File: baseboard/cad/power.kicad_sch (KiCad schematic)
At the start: 37 parts, among them J6 2P_HEADER, J7 2P_HEADER, U7 TLV767, U8 LT3463, U9 LT3032

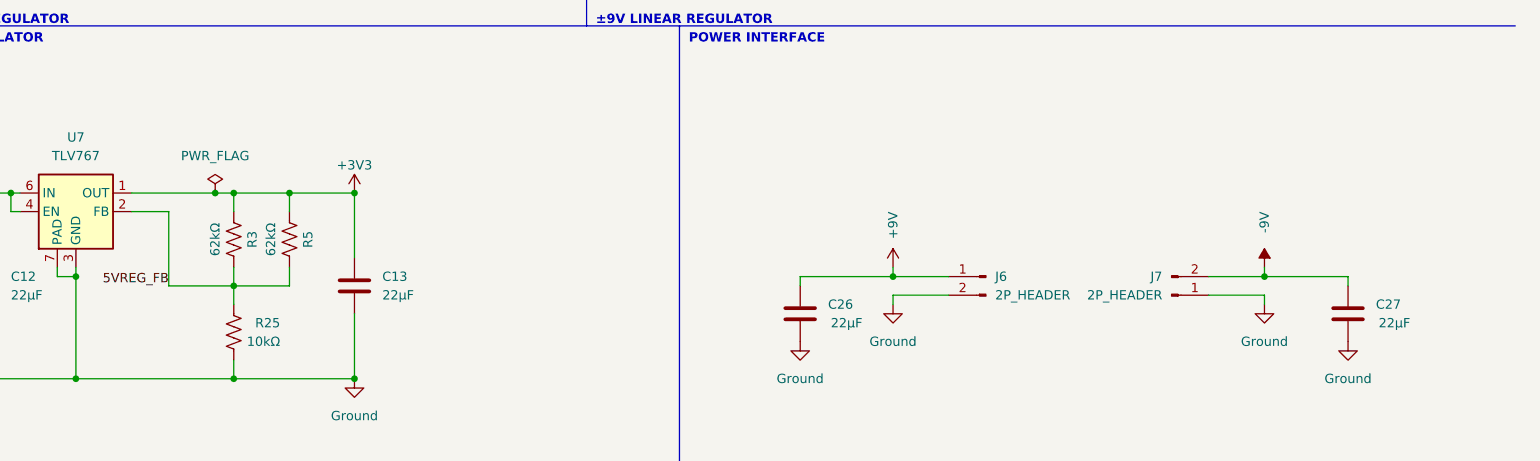
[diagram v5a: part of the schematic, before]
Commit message: updated schematic page setup
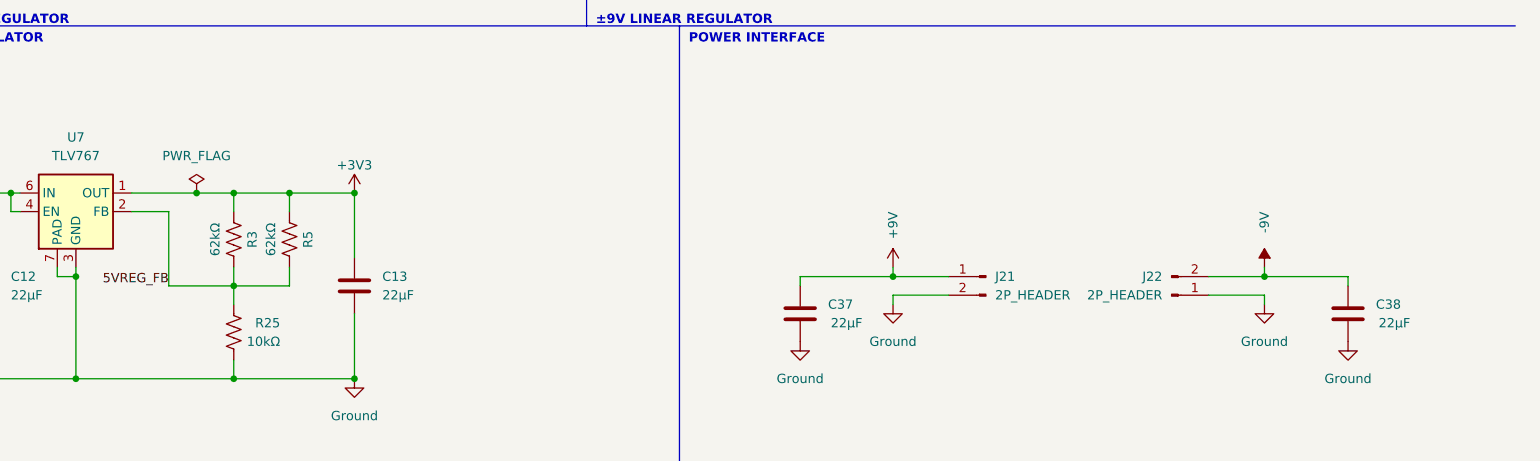
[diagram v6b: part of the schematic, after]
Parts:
- renumbered C26 to C37, C27 to C38, J6 to J21, J7 to J22
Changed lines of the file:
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@@
   (junction (at 219.71 135.89) (diameter 0) (color 0 0 0 0)
   )
+  (junction (at 73.66 124.46) (diameter 0) (color 0 0 0 0)
+  )
   (junction (at 226.06 58.42) (diameter 0) (color 0 0 0 0)
   )
@@
   (junction (at 91.44 38.1) (diameter 0) (color 0 0 0 0)
   )
-  (junction (at 76.2 124.46) (diameter 0) (color 0 0 0 0)
-  )
   (junction (at 156.21 43.18) (diameter 0) (color 0 0 0 0)
   )
@@
     (stroke (width 0) (type default))
   )
+  (wire (pts (xy 73.66 124.46) (xy 78.74 124.46))
+    (stroke (width 0) (type default))
+  )
   (wire (pts (xy 78.74 147.32) (xy 78.74 149.86))
     (stroke (width 0) (type default))
@@
     (stroke (width 0) (type default))
   )
+  (wire (pts (xy 78.74 137.16) (xy 86.36 137.16))
+    (stroke (width 0) (type default))
+  )
   (wire (pts (xy 219.71 134.62) (xy 219.71 135.89))
     (stroke (width 0) (type default))
@@
     (stroke (width 0) (type default))
   )
-  (wire (pts (xy 64.77 124.46) (xy 76.2 124.46))
+  (wire (pts (xy 64.77 124.46) (xy 73.66 124.46))
     (stroke (width 0) (type default))
   )
@@
     (stroke (width 0) (type default))
   )
-  (wire (pts (xy 78.74 137.16) (xy 86.36 137.16))
-    (stroke (width 0) (type default))
-  )
   (wire (pts (xy 114.3 58.42) (xy 114.3 59.69))
     (stroke (width 0) (type default))
@@
   )
   (wire (pts (xy 39.37 53.34) (xy 39.37 58.42))
-    (stroke (width 0) (type default))
-  )
-  (wire (pts (xy 76.2 124.46) (xy 78.74 124.46))
     (stroke (width 0) (type default))
   )
@@
     )
   )
+  (netclass_flag "" (length 2.54) (shape round) (at 69.85 137.16 180) (fields_autoplaced)
+    (effects (font (size 1.27 1.27)) (justify right bottom))
+    (property "Power" "Power" (at 70.5485 139.7 0)
+      (effects (font (size 1.27 1.27) italic) (justify left))
+    )
+  )
+  (netclass_flag "" (length 2.54) (shape round) (at 191.77 73.66 180) (fields_autoplaced)
+    (effects (font (size 1.27 1.27)) (justify right bottom))
+    (property "Power" "Power" (at 192.4685 76.2 0)
+      (effects (font (size 1.27 1.27) italic) (justify left))
+    )
+  )
+  (netclass_flag "" (length 2.54) (shape round) (at 228.6 78.74 180) (fields_autoplaced)
+    (effects (font (size 1.27 1.27)) (justify right bottom))
+    (property "Power" "Power" (at 229.2985 81.28 0)
+      (effects (font (size 1.27 1.27) italic) (justify left))
+    )
+  )
+  (netclass_flag "" (length 2.54) (shape round) (at 76.2 124.46 0) (fields_autoplaced)
+    (effects (font (size 1.27 1.27)) (justify left bottom))
+    (property "Power" "Power" (at 76.8985 121.92 0)
+      (effects (font (size 1.27 1.27) italic) (justify left))
+    )
+  )
+  (netclass_flag "" (length 2.54) (shape round) (at 48.26 53.34 180) (fields_autoplaced)
+    (effects (font (size 1.27 1.27)) (justify right bottom))
+    (property "Power" "Power" (at 48.9585 55.88 0)
+      (effects (font (size 1.27 1.27) italic) (justify left))
+    )
+  )
+  (netclass_flag "" (length 2.54) (shape round) (at 86.36 45.72 180) (fields_autoplaced)
+    (effects (font (size 1.27 1.27)) (justify right bottom))
+    (property "Power" "Power" (at 87.0585 48.26 0)
+      (effects (font (size 1.27 1.27) italic) (justify left))
+    )
+  )
+  (netclass_flag "" (length 2.54) (shape round) (at 93.98 38.1 0) (fields_autoplaced)
+    (effects (font (size 1.27 1.27)) (justify left bottom))
+    (property "Power" "Power" (at 94.6785 35.56 0)
+      (effects (font (size 1.27 1.27) italic) (justify left))
+    )
+  )
+  (netclass_flag "" (length 2.54) (shape round) (at 228.6 38.1 0) (fields_autoplaced)
+    (effects (font (size 1.27 1.27)) (justify left bottom))
+    (property "Power" "Power" (at 229.2985 35.56 0)
+      (effects (font (size 1.27 1.27) italic) (justify left))
+    )
+  )
+  (netclass_flag "" (length 2.54) (shape round) (at 39.37 78.74 180) (fields_autoplaced)
+    (effects (font (size 1.27 1.27)) (justify right bottom))
+    (property "Power" "Power" (at 40.0685 81.28 0)
+      (effects (font (size 1.27 1.27) italic) (justify left))
+    )
+  )
+  (netclass_flag "" (length 3.78) (shape round) (at 85.09 58.42 0) (fields_autoplaced)
+    (effects (font (size 1.27 1.27)) (justify left bottom))
+    (property "Power" "Power" (at 85.7885 54.64 0)
+      (effects (font (size 1.27 1.27) italic) (justify left))
+    )
+  )
+  (netclass_flag "" (length 2.54) (shape round) (at 93.98 78.74 180) (fields_autoplaced)
+    (effects (font (size 1.27 1.27)) (justify right bottom))
+    (property "Power" "Power" (at 94.6785 81.28 0)
+      (effects (font (size 1.27 1.27) italic) (justify left))
+    )
+  )
+  (netclass_flag "" (length 2.54) (shape round) (at 86.36 53.34 0) (fields_autoplaced)
+    (effects (font (size 1.27 1.27)) (justify left bottom))
+    (property "Power" "Power" (at 87.0585 50.8 0)
+      (effects (font (size 1.27 1.27) italic) (justify left))
+    )
+  )
+  (netclass_flag "" (length 2.54) (shape round) (at 48.26 58.42 180) (fields_autoplaced)
+    (effects (font (size 1.27 1.27)) (justify right bottom))
+    (property "Power" "Power" (at 48.9585 60.96 0)
+      (effects (font (size 1.27 1.27) italic) (justify left))
+    )
+  )
+  (netclass_flag "" (length 2.54) (shape round) (at 191.77 43.18 180) (fields_autoplaced)
+    (effects (font (size 1.27 1.27)) (justify right bottom))
+    (property "Power" "Power" (at 192.4685 45.72 0)
+      (effects (font (size 1.27 1.27) italic) (justify left))
+    )
+  )
+  (netclass_flag "" (length 2.54) (shape round) (at 86.36 63.5 180) (fields_autoplaced)
+    (effects (font (size 1.27 1.27)) (justify right bottom))
+    (property "Power" "Power" (at 87.0585 66.04 0)
+      (effects (font (size 1.27 1.27) italic) (justify left))
+    )
+  )
   (symbol (lib_id "Connector:Conn_01x02_Male") (at 181.61 135.89 0) (mirror y) (unit 1)
     (in_bom yes) (on_board yes) (dnp no) (fields_autoplaced)
-    (property "Reference" "J6" (at 182.88 135.8899 0)
+    (property "Reference" "J21" (at 182.88 135.8899 0)
       (effects (font (size 1.27 1.27)) (justify right))
     )
@@
     )
   )
-  (symbol (lib_name "PWR_FLAG_3") (lib_id "power:PWR_FLAG") (at 76.2 124.46 0) (unit 1)
+  (symbol (lib_name "PWR_FLAG_3") (lib_id "power:PWR_FLAG") (at 73.66 124.46 0) (unit 1)
     (in_bom yes) (on_board yes) (dnp no) (fields_autoplaced)
-    (property "Reference" "#FLG03" (at 76.2 122.555 0)
-      (effects (font (size 1.27 1.27)) hide)
-    )
-    (property "Value" "PWR_FLAG" (at 76.2 119.38 0)
-      (effects (font (size 1.27 1.27)))
-    )
-    (property "Footprint" "" (at 76.2 124.46 0)
-      (effects (font (size 1.27 1.27)) hide)
-    )
-    (property "Datasheet" "~" (at 76.2 124.46 0)
+    (property "Reference" "#FLG03" (at 73.66 122.555 0)
+      (effects (font (size 1.27 1.27)) hide)
+    )
+    (property "Value" "PWR_FLAG" (at 73.66 119.38 0)
+      (effects (font (size 1.27 1.27)))
+    )
+    (property "Footprint" "" (at 73.66 124.46 0)
+      (effects (font (size 1.27 1.27)) hide)
+    )
+    (property "Datasheet" "~" (at 73.66 124.46 0)
       (effects (font (size 1.27 1.27)) hide)
     )
@@
   (symbol (lib_id "Library:Ground") (at 156.21 144.78 0) (unit 1)
     (in_bom yes) (on_board yes) (dnp no)
-    (property "Reference" "#PWR018" (at 156.21 151.13 0)
+    (property "Reference" "#PWR047" (at 156.21 151.13 0)
       (effects (font (size 1.27 1.27)) hide)
     )
@@
   (symbol (lib_id "Device:C") (at 156.21 140.97 180) (unit 1)
     (in_bom yes) (on_board yes) (dnp no)
-    (property "Reference" "C26" (at 160.02 139.7 0)
+    (property "Reference" "C37" (at 160.02 139.7 0)
       (effects (font (size 1.27 1.27)) (justify right))
     )
@@
   (symbol (lib_id "Device:C") (at 231.14 140.97 180) (unit 1)
     (in_bom yes) (on_board yes) (dnp no)
-    (property "Reference" "C27" (at 234.95 139.7 0)
+    (property "Reference" "C38" (at 234.95 139.7 0)
       (effects (font (size 1.27 1.27)) (justify right))
     )
@@
   (symbol (lib_id "power:+9V") (at 168.91 134.62 0) (unit 1)
     (in_bom yes) (on_board yes) (dnp no)
-    (property "Reference" "#PWR019" (at 168.91 138.43 0)
+    (property "Reference" "#PWR052" (at 168.91 138.43 0)
       (effects (font (size 1.27 1.27)) hide)
     )
@@
   (symbol (lib_id "Library:Ground") (at 219.71 139.7 0) (mirror y) (unit 1)
     (in_bom yes) (on_board yes) (dnp no)
-    (property "Reference" "#PWR022" (at 219.71 146.05 0)
+    (property "Reference" "#PWR058" (at 219.71 146.05 0)
       (effects (font (size 1.27 1.27)) hide)
     )
@@
   (symbol (lib_id "Library:Ground") (at 231.14 144.78 0) (unit 1)
     (in_bom yes) (on_board yes) (dnp no)
-    (property "Reference" "#PWR023" (at 231.14 151.13 0)
+    (property "Reference" "#PWR059" (at 231.14 151.13 0)
       (effects (font (size 1.27 1.27)) hide)
     )
@@
   (symbol (lib_id "Library:Ground") (at 168.91 139.7 0) (unit 1)
     (in_bom yes) (on_board yes) (dnp no)
-    (property "Reference" "#PWR020" (at 168.91 146.05 0)
+    (property "Reference" "#PWR056" (at 168.91 146.05 0)
       (effects (font (size 1.27 1.27)) hide)
     )
@@
   (symbol (lib_id "Connector:Conn_01x02_Male") (at 207.01 138.43 0) (mirror x) (unit 1)
     (in_bom yes) (on_board yes) (dnp no) (fields_autoplaced)
-    (property "Reference" "J7" (at 205.74 135.8899 0)
+    (property "Reference" "J22" (at 205.74 135.8899 0)
       (effects (font (size 1.27 1.27)) (justify right))
     )
@@
   (symbol (lib_id "power:-9V") (at 219.71 134.62 0) (unit 1)
     (in_bom yes) (on_board yes) (dnp no)
-    (property "Reference" "#PWR021" (at 219.71 137.795 0)
-      (effects (font (size 1.27 1.27)) hide)
-    )
+    (property "Reference" "#PWR057" (at 219.71 137.795 0)
+      (effects (font (size 1.27 1.27)) hide)
+    )

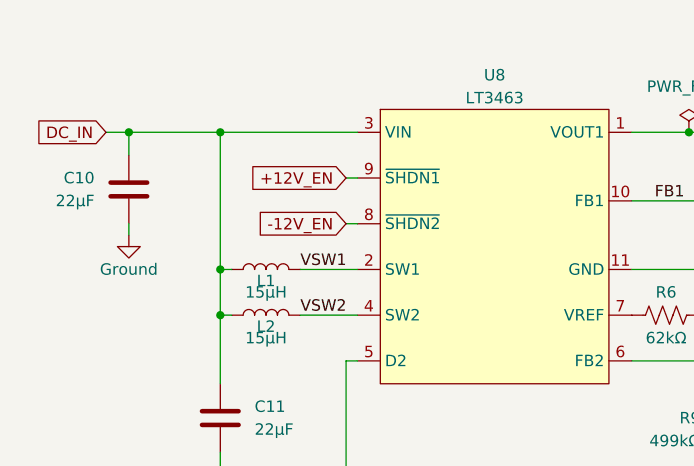
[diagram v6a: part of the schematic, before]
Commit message: cleaning up layout, added graphic symbols
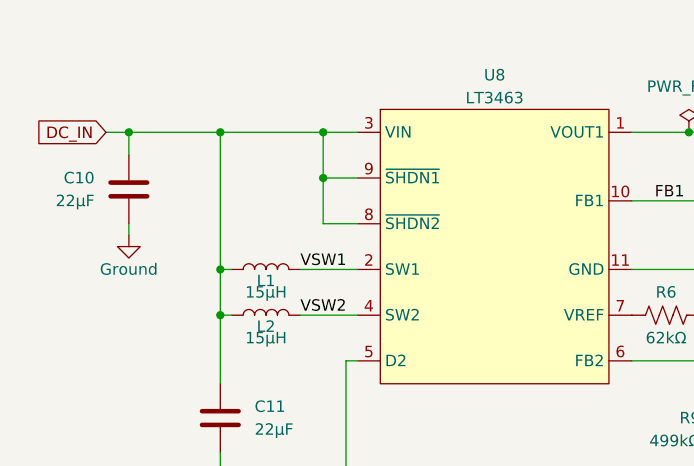
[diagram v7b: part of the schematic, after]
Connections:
- net +12V_EN is gone; now on net DC_IN: U8.9 (~{SHDN1})
- net -12V_EN is gone; now on net DC_IN: U8.8 (~{SHDN2})
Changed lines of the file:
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@@
   (junction (at 158.75 78.74) (diameter 0) (color 0 0 0 0)
   )
+  (junction (at 50.8 43.18) (diameter 0) (color 0 0 0 0)
+  )
   (junction (at 156.21 38.1) (diameter 0) (color 0 0 0 0)
   )
@@
   (junction (at 29.21 38.1) (diameter 0) (color 0 0 0 0)
   )
+  (junction (at 50.8 38.1) (diameter 0) (color 0 0 0 0)
+  )
   (junction (at 207.01 38.1) (diameter 0) (color 0 0 0 0)
   )
@@
     (stroke (width 0) (type default))
   )
-  (wire (pts (xy 53.34 48.26) (xy 54.61 48.26))
+  (wire (pts (xy 50.8 48.26) (xy 54.61 48.26))
     (stroke (width 0) (type default))
   )
@@
     (stroke (width 0) (type default))
   )
-  (wire (pts (xy 39.37 38.1) (xy 54.61 38.1))
+  (wire (pts (xy 39.37 38.1) (xy 50.8 38.1))
     (stroke (width 0) (type default))
   )
@@
     (stroke (width 0) (type default))
   )
+  (wire (pts (xy 50.8 43.18) (xy 50.8 38.1))
+    (stroke (width 0) (type default))
+  )
   (wire (pts (xy 140.97 38.1) (xy 146.05 38.1))
     (stroke (width 0) (type default))
@@
     (stroke (width 0) (type default))
   )
+  (wire (pts (xy 50.8 48.26) (xy 50.8 43.18))
+    (stroke (width 0) (type default))
+  )
   (wire (pts (xy 64.77 124.46) (xy 73.66 124.46))
     (stroke (width 0) (type default))
@@
     (stroke (width 0) (type default))
   )
-  (wire (pts (xy 53.34 43.18) (xy 54.61 43.18))
+  (wire (pts (xy 50.8 43.18) (xy 54.61 43.18))
+    (stroke (width 0) (type default))
+  )
+  (wire (pts (xy 50.8 38.1) (xy 54.61 38.1))
     (stroke (width 0) (type default))
   )
@@
     )
   )
-  (global_label "+12V_EN" (shape input) (at 53.34 43.18 180) (fields_autoplaced)
-    (effects (font (size 1.27 1.27)) (justify right))
-    (property "Intersheetrefs" "${INTERSHEET_REFS}" (at 43.1166 43.18 0)
-      (effects (font (size 1.27 1.27)) (justify right) hide)
-    )
-  )
   (global_label "+Vsw" (shape input) (at 115.57 38.1 0) (fields_autoplaced)
     (effects (font (size 1.27 1.27)) (justify left))
@@
       (effects (font (size 1.27 1.27)) (justify right) hide)
     )
-  )
-  (global_label "-12V_EN" (shape input) (at 53.34 48.26 180) (fields_autoplaced)
-    (effects (font (size 1.27 1.27)) (justify right))
-    (property "Intersheetrefs" "${INTERSHEET_REFS}" (at 43.1166 48.26 0)
-      (effects (font (size 1.27 1.27)) (justify right) hide)
-    )
